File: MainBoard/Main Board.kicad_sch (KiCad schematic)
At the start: 64 parts, among them IC1 TLV61070ADBVR, J1 Motor, J2 Motor, J3 Row 2, J4 Row 2, J5 USB PowerOnly 6P, J8 FFC Connector, Q1 NMOS, Q2 NMOS, SW1 SS12D10G5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

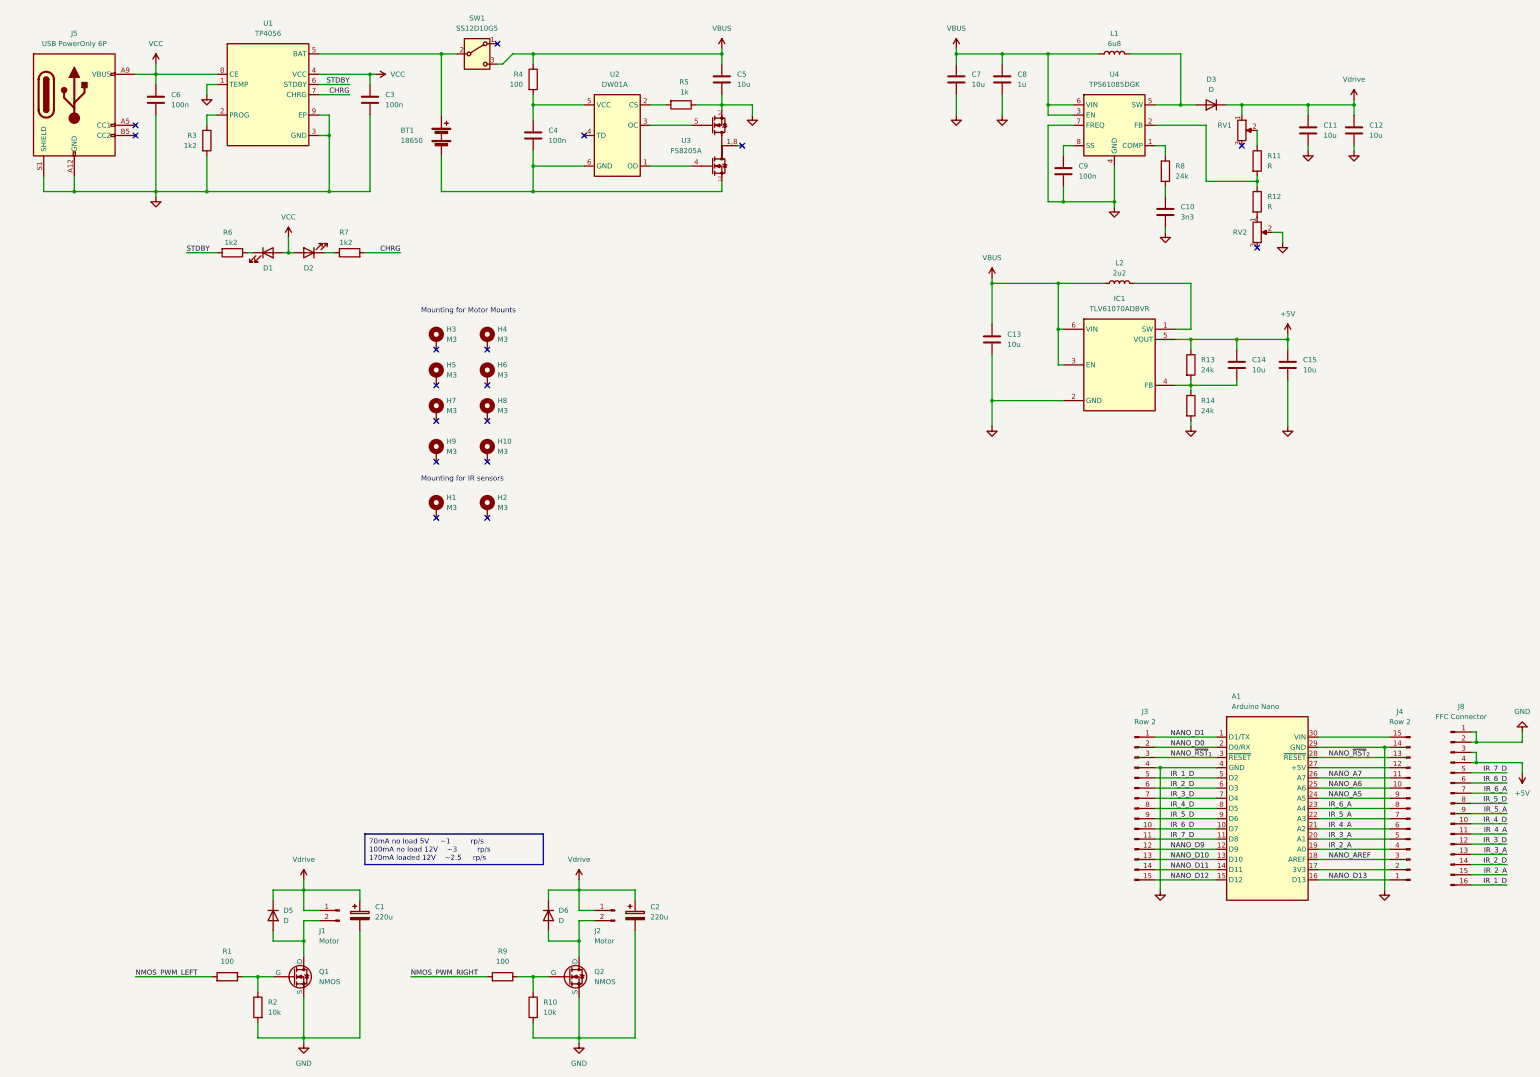
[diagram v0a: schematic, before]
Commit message: Cleaned up MainBoard Schematic
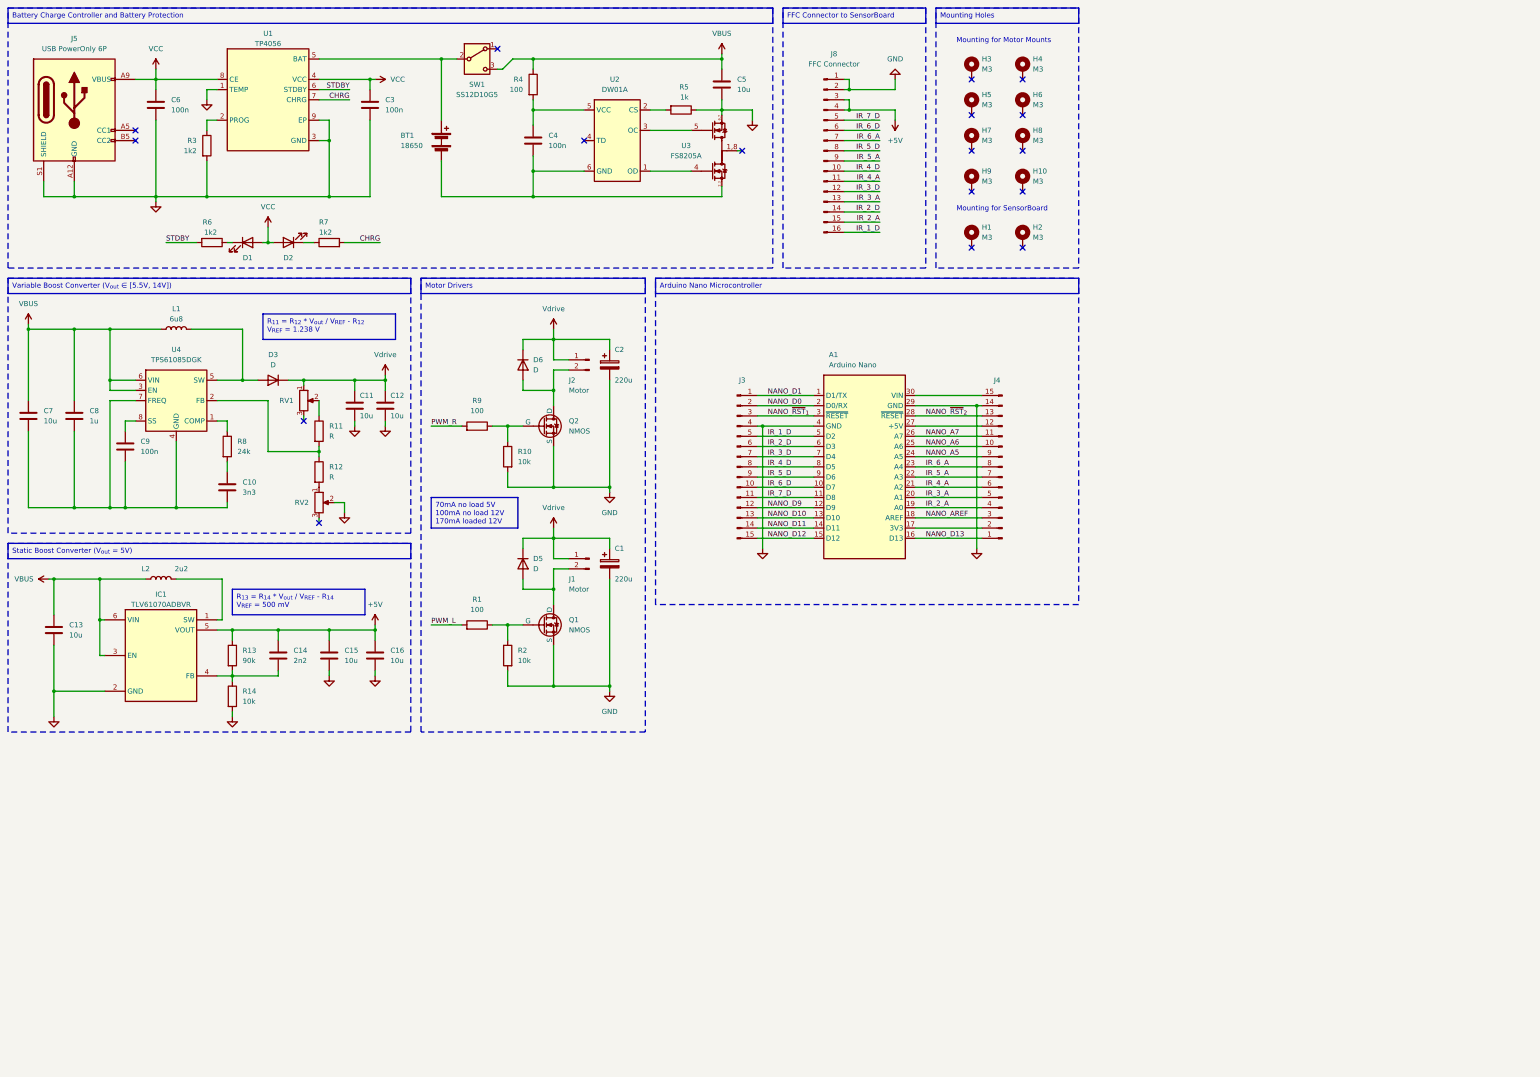
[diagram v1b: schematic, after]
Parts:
- added C16: 10u, symbol Device:C
- C14: value 10u -> 2n2
- L2: footprint Inductor_SMD:L_6.3x6.3_H3 -> Inductor_SMD:L_Changjiang_FNR5030S
- R13: value 24k -> 90k
- R14: value 24k -> 10k
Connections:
- net +5V: now also C16.1
- net GND: now also C16.2; no longer C10.2, C7.2, C8.2, C9.2, U4.4 (GND), U4.7 (FREQ)
- net NMOS_PWM_LEFT renamed PWM_L
- net NMOS_PWM_RIGHT renamed PWM_R
- new net: C10.2, C7.2, C8.2, C9.2, U4.4 (GND), U4.7 (FREQ)
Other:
- note added: "Mounting for SensorBoard"
- note removed: "Mounting for IR sensors"
- moved on the sheet: A1, BT1, C1, C10, C11, C12, C13, C15, C2, C3, C4, C5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

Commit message: Small Changes to mainboard schematic
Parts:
- removed D3: D, symbol Device:D
- removed D5, D6: D, Diode_THT:D_DO-15_P10.16mm_Horizontal, symbol Device:D
- added D3, D4, D5, D6: PMEG2010AEH, Diode_SMD:D_SOD-123F, symbol Diode:PMEG2010AEH
- C10, C14, C3, C4, C6, C8, C9: footprint (none) -> Capacitor_SMD:C_0402_1005Metric
- C11, C12, C13, C15, C16, C5, C7: footprint (none) -> Capacitor_SMD:C_0603_1608Metric
- D1, D2: footprint (none) -> LED_SMD:LED_0603_1608Metric
- R11, R12, R13, R14, R3, R5, R6, R7, R8: footprint (none) -> Resistor_SMD:R_0402_1005Metric
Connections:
- net NANO_D10 is gone; now on net PWM_L: A1.13 (D10), J3.13 (Pin_13)
- net NANO_D9 is gone; now on net PWM_R: A1.12 (D9), J3.12 (Pin_12)
- net +5V: now also D6.2 (A)
- net Vdrive: now also D3.1 (K), D4.1 (K), D5.1 (K)
- net at J2.2 (Pin_2), Q2.1 (D): now also D3.2 (A)
- net at L1.2, U4.5 (SW): now also D4.2 (A)
- net at A1.30 (VIN), J4.15 (Pin_15): now also D6.1 (K)
- net at J1.2 (Pin_2), Q1.1 (D): now also D5.2 (A)

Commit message: Updated Mainboard
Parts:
- RV1, RV2: footprint (none) -> Potentiometer_SMD:Potentiometer_Bourns_TC33X_Vertical
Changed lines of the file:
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@@
       (effects (font (size 1.27 1.27)) (justify right) hide)
     )
-    (property "Footprint" "" (at 92.71 137.16 0)
+    (property "Footprint" "Potentiometer_SMD:Potentiometer_Bourns_TC33X_Vertical" (at 92.71 137.16 0)
       (effects (font (size 1.27 1.27)) hide)
     )
@@
       (effects (font (size 1.27 1.27)) (justify right) hide)
     )
-    (property "Footprint" "" (at 88.9 111.76 0)
-      (effects (font (size 1.27 1.27)) hide)
-    )
+    (property "Footprint" "Potentiometer_SMD:Potentiometer_Bourns_TC33X_Vertical" (at 88.9 111.76 0)
+      (effects (font (size 1.27 1.27)) hide)
+    )

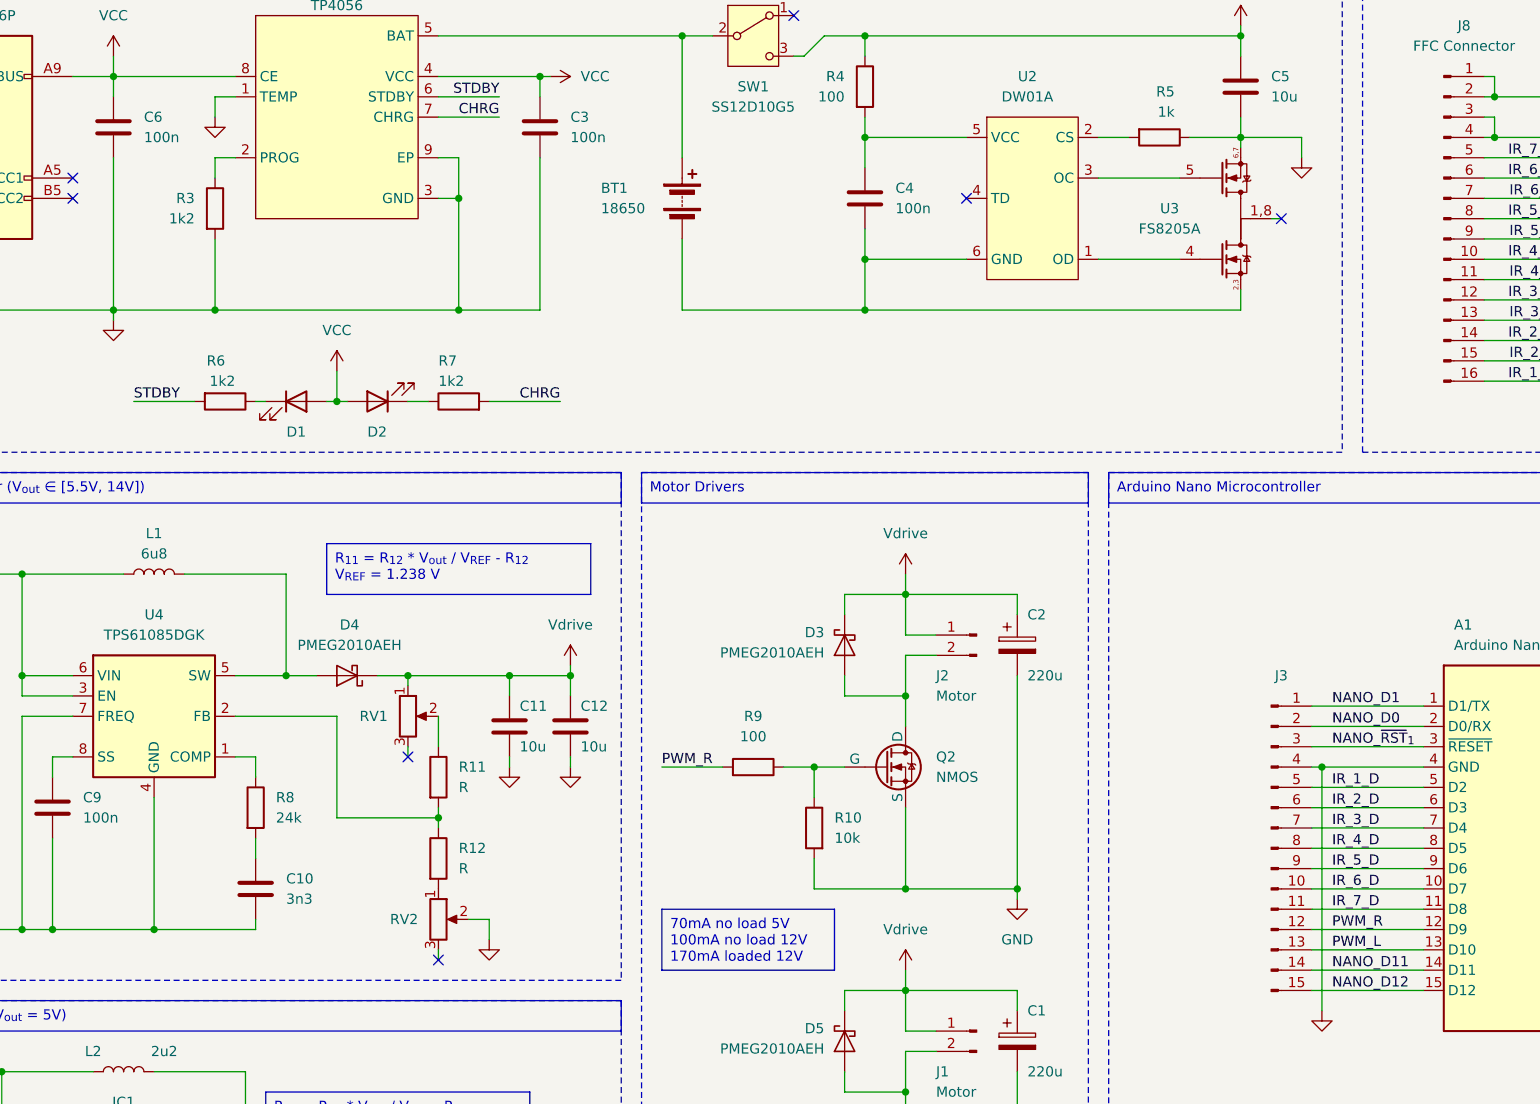
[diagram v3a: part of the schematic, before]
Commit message: Main board pcb traced
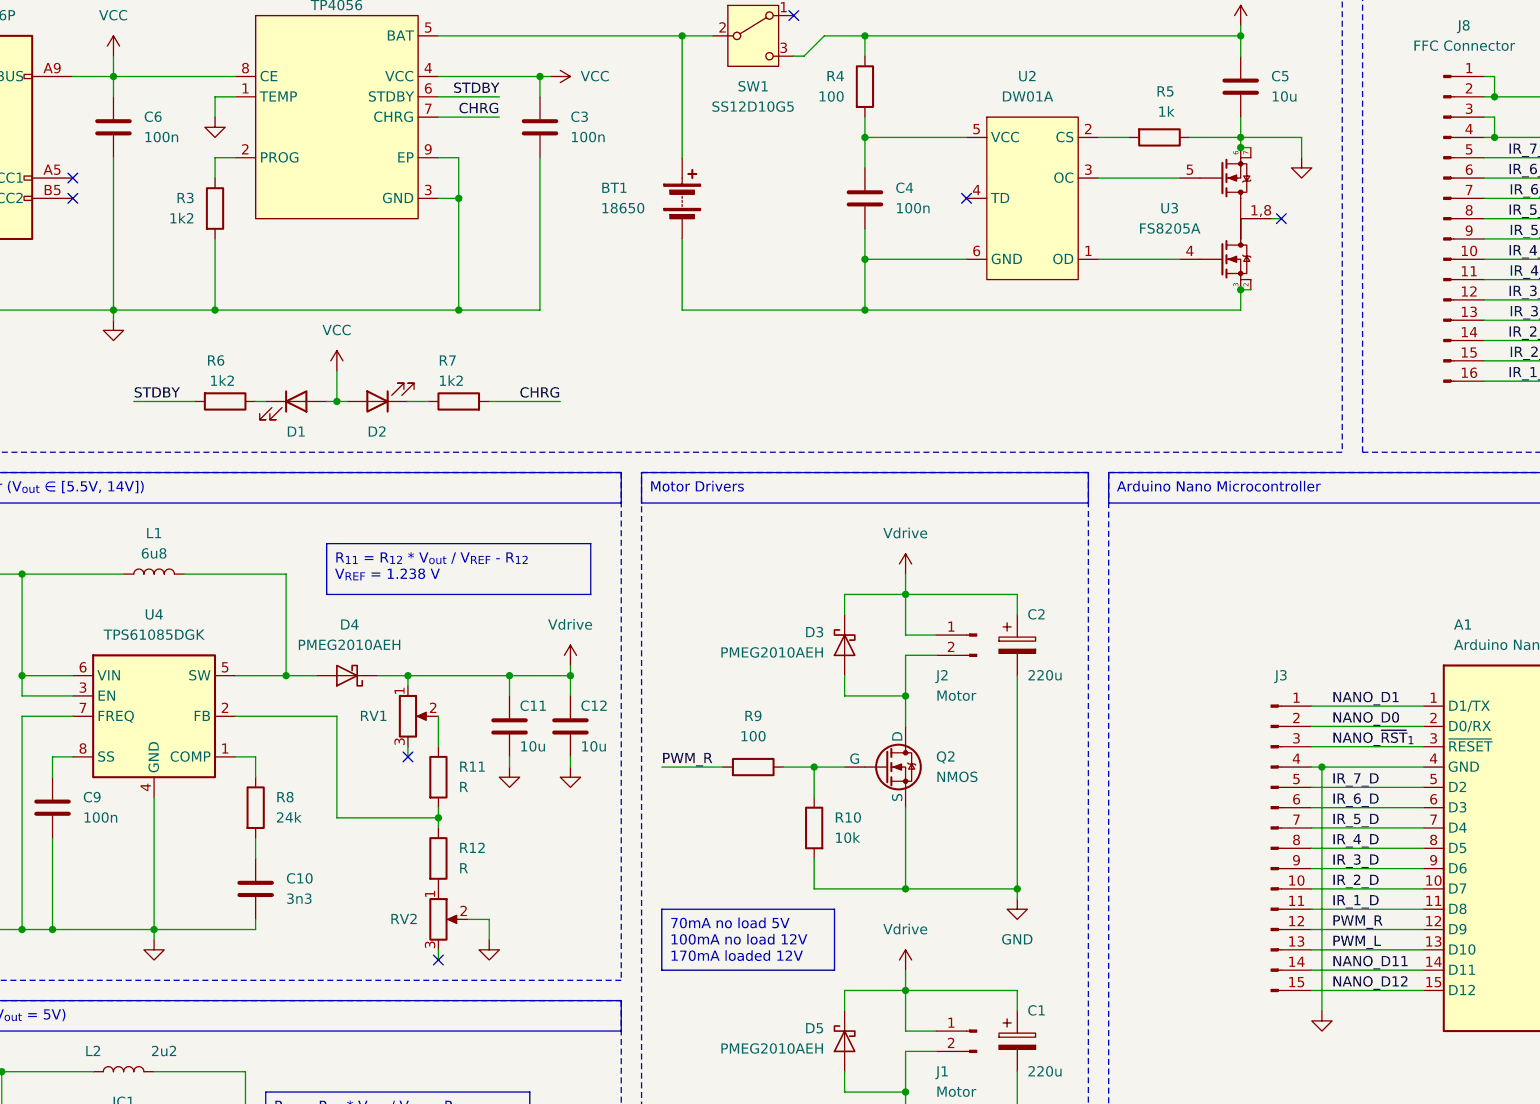
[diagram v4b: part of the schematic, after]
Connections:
- net GND: now also C10.2, C7.2, C8.2, C9.2, U3.6, U3.7, U4.4 (GND), U4.7 (FREQ); no longer U3.6,7
- net IR_1_D: now also A1.11 (D8), J3.11 (Pin_11); no longer A1.5 (D2), J3.5 (Pin_5)
- net IR_2_D: now also A1.10 (D7), J3.10 (Pin_10); no longer A1.6 (D3), J3.6 (Pin_6)
- net IR_3_D: now also A1.9 (D6), J3.9 (Pin_9); no longer A1.7 (D4), J3.7 (Pin_7)
- net IR_5_D: now also A1.7 (D4), J3.7 (Pin_7); no longer A1.9 (D6), J3.9 (Pin_9)
- net IR_6_D: now also A1.6 (D3), J3.6 (Pin_6); no longer A1.10 (D7), J3.10 (Pin_10)
- net IR_7_D: now also A1.5 (D2), J3.5 (Pin_5); no longer A1.11 (D8), J3.11 (Pin_11)
- net at D3.2 (A), J2.2 (Pin_2): now also Q2.2 (D); no longer Q2.1 (D)
- net at BT1.2 (-), C4.2, U2.6 (GND): now also U3.2, U3.3; no longer U3.2,3
- net at D5.2 (A), J1.2 (Pin_2): now also Q1.2 (D); no longer Q1.1 (D)
- net at R10.1, R9.1: now also Q2.1 (G); no longer Q2.2 (G)
- net at R1.1, R2.1: now also Q1.1 (G); no longer Q1.2 (G)
